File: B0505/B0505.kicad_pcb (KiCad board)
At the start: 2 copper layers, 39.7 x 26.7 mm, 26 parts, among them J1 CN-TB-3.5MM-2P-M-TH-ST, J2 CN-BERG-2.54MM-2P-M-TH-ST, J3 CN-BERG-2.54MM-2P-M-TH-ST, J4 CN-TB-3.5MM-2P-M-TH-ST

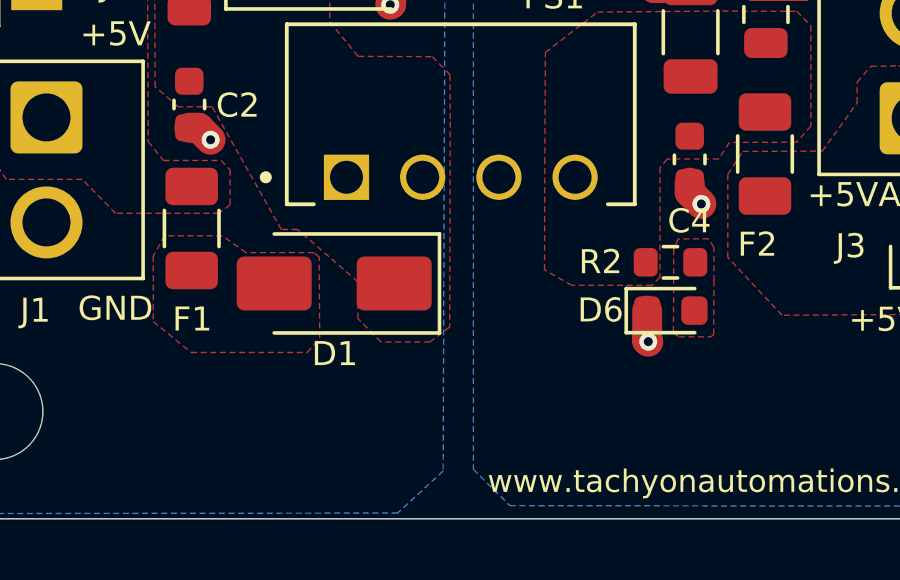
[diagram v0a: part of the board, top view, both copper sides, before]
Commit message: moved holes and changed gnd near d6
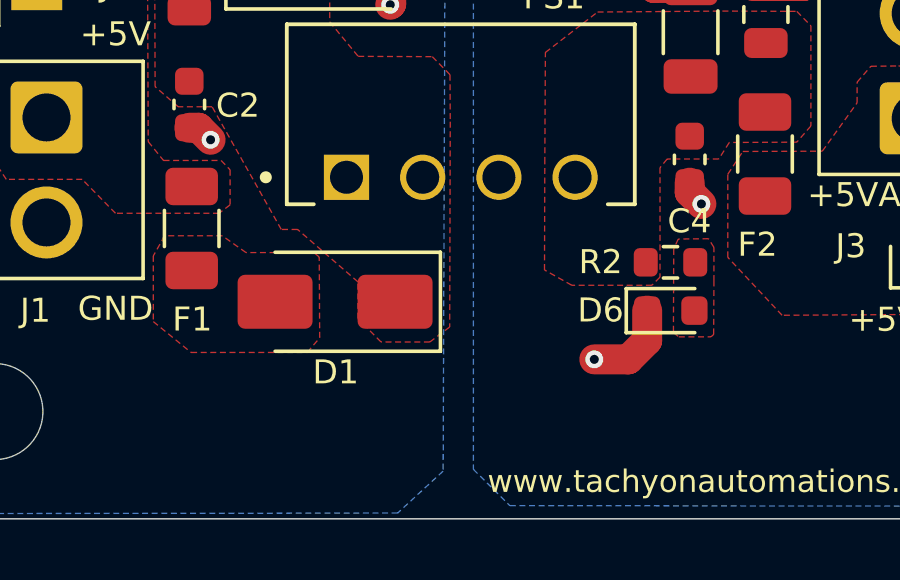
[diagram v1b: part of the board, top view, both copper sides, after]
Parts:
- moved D1 0.61 mm to (186.1, 74.5)
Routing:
- net GNDA: track 4.52 -> 6.49 mm
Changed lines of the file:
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@@
 	(footprint "Diode_SMD:D_SMA"
 		(layer "F.Cu")
-		(at 186.03 73.87 180)
+		(at 186.06 74.48 180)
 		(descr "Diode SMA (DO-214AC)")
 		(tags "Diode SMA (DO-214AC)")
@@
 	)
 	(segment
+		(start 194.7 76.4)
+		(end 195.835 76.4)
+		(width 1)
+		(layer "F.Cu")
+		(net 4)
+	)
+	(segment
 		(start 196.4625 75.7725)
-		(end 196.5 75.81)
+		(end 196.4625 74.775)
 		(width 1)
 		(layer "F.Cu")
@@
 	)
 	(segment
-		(start 196.4625 74.775)
-		(end 196.4625 75.7725)
+		(start 196.69 64.02)
+		(end 196.63 63.96)
 		(width 1)
 		(layer "F.Cu")
@@
 	)
 	(segment
-		(start 196.69 64.02)
-		(end 196.63 63.96)
+		(start 197.88 70.51)
+		(end 197.88 70.83)
 		(width 1)
 		(layer "F.Cu")
@@
 	)
 	(segment
-		(start 197.88 70.51)
-		(end 197.88 70.83)
+		(start 195.835 76.4)
+		(end 196.4625 75.7725)
 		(width 1)
 		(layer "F.Cu")
@@
 	)
 	(via
-		(at 196.5 75.81)
+		(at 194.7 76.4)
 		(size 0.6)
 		(drill 0.3)

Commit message: moved ps1
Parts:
- moved PS1 8.64 mm to (189.9, 59.6)
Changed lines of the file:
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@@
 		(tags "Diode SMA (DO-214AC)")
 		(property "Reference" "D1"
-			(at -0.02 -2.35 180)
+			(at 0 -2.32 180)
 			(layer "F.SilkS")
 			(effects
@@
 	(footprint "Tachyon_Library:CONV_B0505S-1WR3-TH"
 		(layer "F.Cu")
-		(at 190.25 68.23)
+		(at 189.88 59.6)
 		(property "Reference" "PS1"
 			(at 3.11 -3.9 0)
